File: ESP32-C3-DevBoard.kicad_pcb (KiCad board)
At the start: 2 copper layers, 25.4 x 26.7 mm, 19 parts, among them J1 USB_C_Receptacle_USB2.0, J2 Conn_01x10, J3 Conn_01x10, SW1 SW_Push, SW2 SW_Push, U1 ESP32-C3-WROOM-02, U2 AMS1117-3.3

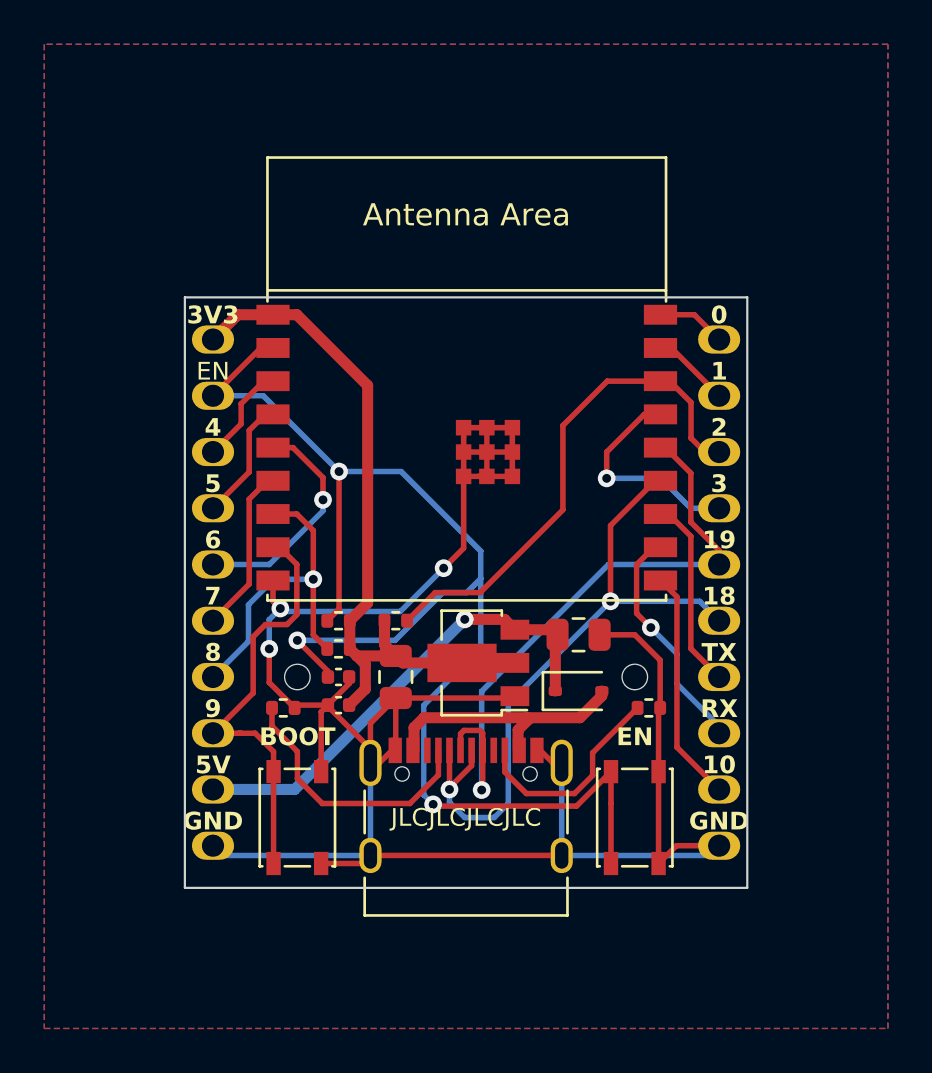
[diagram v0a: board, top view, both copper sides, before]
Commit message: fix silkscreen and tooling hole position
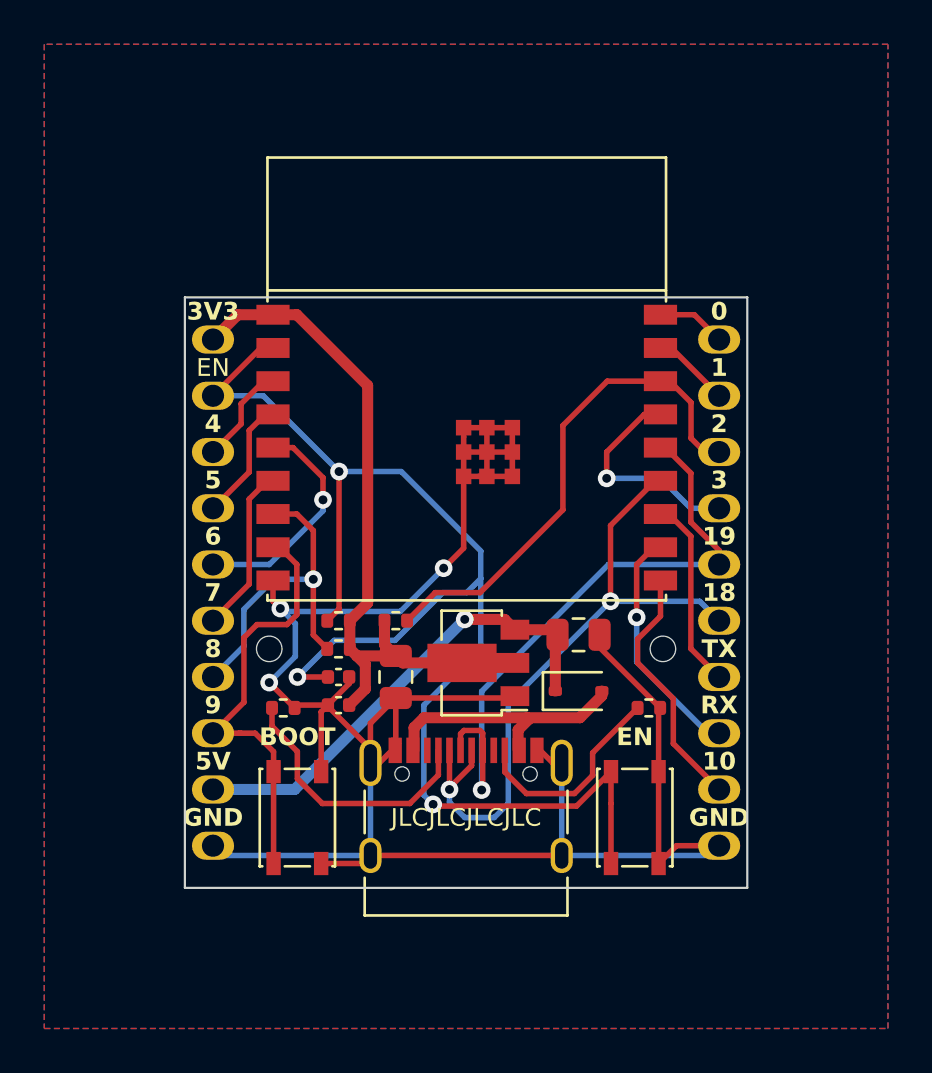
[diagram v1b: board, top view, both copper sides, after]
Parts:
- moved H1 1.80 mm to (137.2, 113.7)
- moved H2 1.80 mm to (154.9, 113.7)
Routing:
- net /IO10: track 10.5 -> 11.4 mm

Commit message: Add files via upload
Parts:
- H1, H2: value MountingHole -> ToolingHole
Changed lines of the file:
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@@
   (title_block
     (title "ESP32-C3 Development Board")
-    (rev "v1.0.0")
+    (rev "v1.0.1")
   )
   (layers
@@
     (pad "2" smd roundrect (at 0.51 0) (size 0.54 0.64) (layers "F.Cu" "F.Paste" "F.Mask") (roundrect_rratio 0.25)
       (net 15 "/IO2") (pintype "passive"))
-    (model "${KICAD6_3DMODEL_DIR}/Resistor_SMD.3dshapes/R_0402_1005Metric.wrl"
+    (model "${KICAD7_3DMODEL_DIR}/Resistor_SMD.3dshapes/R_0402_1005Metric.wrl"
       (offset (xyz 0 0 0))
       (scale (xyz 1 1 1))
@@
     (pad "2" smd roundrect (at 0.51 0 180) (size 0.54 0.64) (layers "F.Cu" "F.Paste" "F.Mask") (roundrect_rratio 0.25)
       (net 6 "/IO8") (pintype "passive"))
-    (model "${KICAD6_3DMODEL_DIR}/Resistor_SMD.3dshapes/R_0402_1005Metric.wrl"
+    (model "${KICAD7_3DMODEL_DIR}/Resistor_SMD.3dshapes/R_0402_1005Metric.wrl"
       (offset (xyz 0 0 0))
       (scale (xyz 1 1 1))
@@
     (pad "2" smd roundrect (at 0.95 0 270) (size 1 1.45) (layers "F.Cu" "F.Paste" "F.Mask") (roundrect_rratio 0.25)
       (net 8 "GND") (pintype "passive"))
-    (model "${KICAD6_3DMODEL_DIR}/Capacitor_SMD.3dshapes/C_0805_2012Metric.wrl"
+    (model "${KICAD7_3DMODEL_DIR}/Capacitor_SMD.3dshapes/C_0805_2012Metric.wrl"
       (offset (xyz 0 0 0))
       (scale (xyz 1 1 1))
@@
     (pad "2" smd roundrect (at 0.48 0) (size 0.56 0.62) (layers "F.Cu" "F.Paste" "F.Mask") (roundrect_rratio 0.25)
       (net 18 "+3V3") (pintype "passive"))
-    (model "${KICAD6_3DMODEL_DIR}/Capacitor_SMD.3dshapes/C_0402_1005Metric.wrl"
+    (model "${KICAD7_3DMODEL_DIR}/Capacitor_SMD.3dshapes/C_0402_1005Metric.wrl"
       (offset (xyz 0 0 0))
       (scale (xyz 1 1 1))
@@
     (pad "2" smd roundrect (at 0.51 0) (size 0.54 0.64) (layers "F.Cu" "F.Paste" "F.Mask") (roundrect_rratio 0.25)
       (net 8 "GND") (pintype "passive"))
-    (model "${KICAD6_3DMODEL_DIR}/Resistor_SMD.3dshapes/R_0402_1005Metric.wrl"
+    (model "${KICAD7_3DMODEL_DIR}/Resistor_SMD.3dshapes/R_0402_1005Metric.wrl"
       (offset (xyz 0 0 0))
       (scale (xyz 1 1 1))
@@
         (effects (font (size 1 1) (thickness 0.15)))
     )
-    (fp_text value "MountingHole" (at 0 3.2) (layer "F.Fab")
+    (fp_text value "ToolingHole" (at 0 3.2) (layer "F.Fab")
         (effects (font (size 1 1) (thickness 0.15)))
     )
@@
         (effects (font (size 1 1) (thickness 0.15)))
     )
-    (fp_text user "Antenna Area" (at 0 -10.4) (layer "F.SilkS") hide
+    (fp_text user "Antenna Area" (at 0 -10.4) (layer "F.SilkS")
         (effects (font (size 1 1) (thickness 0.15)))
     )
@@
     (pad "2" smd roundrect (at 0.95 0 180) (size 1 1.45) (layers "F.Cu" "F.Paste" "F.Mask") (roundrect_rratio 0.25)
       (net 19 "+5V") (pintype "passive"))
-    (model "${KICAD6_3DMODEL_DIR}/Capacitor_SMD.3dshapes/C_0805_2012Metric.wrl"
+    (model "${KICAD7_3DMODEL_DIR}/Capacitor_SMD.3dshapes/C_0805_2012Metric.wrl"
       (offset (xyz 0 0 0))
       (scale (xyz 1 1 1))
@@
     (pad "2" smd roundrect (at 0.48 0) (size 0.56 0.62) (layers "F.Cu" "F.Paste" "F.Mask") (roundrect_rratio 0.25)
       (net 8 "GND") (pintype "passive"))
-    (model "${KICAD6_3DMODEL_DIR}/Capacitor_SMD.3dshapes/C_0402_1005Metric.wrl"
+    (model "${KICAD7_3DMODEL_DIR}/Capacitor_SMD.3dshapes/C_0402_1005Metric.wrl"
       (offset (xyz 0 0 0))
       (scale (xyz 1 1 1))
@@
         (effects (font (size 1 1) (thickness 0.15)))
     )
-    (fp_text value "MountingHole" (at 0 3.2) (layer "F.Fab")
+    (fp_text value "ToolingHole" (at 0 3.2) (layer "F.Fab")
         (effects (font (size 1 1) (thickness 0.15)))
     )
@@
     (pad "2" smd roundrect (at 1.05 0) (size 0.6 0.45) (layers "F.Cu" "F.Paste" "F.Mask") (roundrect_rratio 0.25)
       (net 20 "VBUS") (pinfunction "A") (pintype "passive"))
-    (model "${KICAD6_3DMODEL_DIR}/Diode_SMD.3dshapes/D_SOD-323.wrl"
+    (model "${KICAD7_3DMODEL_DIR}/Diode_SMD.3dshapes/D_SOD-323.wrl"
       (offset (xyz 0 0 0))
       (scale (xyz 1 1 1))
@@
     (pad "2" smd roundrect (at 0.51 0 180) (size 0.54 0.64) (layers "F.Cu" "F.Paste" "F.Mask") (roundrect_rratio 0.25)
       (net 1 "/EN") (pintype "passive"))
-    (model "${KICAD6_3DMODEL_DIR}/Resistor_SMD.3dshapes/R_0402_1005Metric.wrl"
+    (model "${KICAD7_3DMODEL_DIR}/Resistor_SMD.3dshapes/R_0402_1005Metric.wrl"
       (offset (xyz 0 0 0))
       (scale (xyz 1 1 1))
@@
     (pad "2" smd roundrect (at 0.51 0 180) (size 0.54 0.64) (layers "F.Cu" "F.Paste" "F.Mask") (roundrect_rratio 0.25)
       (net 23 "Net-(J1-CC2)") (pintype "passive"))
-    (model "${KICAD6_3DMODEL_DIR}/Resistor_SMD.3dshapes/R_0402_1005Metric.wrl"
+    (model "${KICAD7_3DMODEL_DIR}/Resistor_SMD.3dshapes/R_0402_1005Metric.wrl"
       (offset (xyz 0 0 0))
       (scale (xyz 1 1 1))
@@
     (pad "3" smd rect (at -1.95 1.5 180) (size 1.3 0.9) (layers "F.Cu" "F.Paste" "F.Mask")
       (net 19 "+5V") (pinfunction "VI") (pintype "power_in"))
-    (model "${KICAD6_3DMODEL_DIR}/Package_TO_SOT_SMD.3dshapes/SOT-89-3.wrl"
+    (model "${KICAD7_3DMODEL_DIR}/Package_TO_SOT_SMD.3dshapes/SOT-89-3.wrl"
       (offset (xyz 0 0 0))
       (scale (xyz 1 1 1))
@@
     (pad "10" thru_hole oval (at 0 -22.86 180) (size 1.905 1.27) (drill 1) (layers "*.Cu" "*.Mask")
       (net 8 "GND") (pinfunction "Pin_10") (pintype "passive"))
-    (model "${KICAD6_3DMODEL_DIR}/Connector_PinHeader_2.54mm.3dshapes/PinHeader_1x10_P2.54mm_Vertical.wrl"
+    (model "${KICAD7_3DMODEL_DIR}/Connector_PinHeader_2.54mm.3dshapes/PinHeader_1x10_P2.54mm_Vertical.wrl"
       (offset (xyz 0 0 0))
       (scale (xyz 1 1 1))
@@
     (pad "10" thru_hole oval (at 0 -22.86 180) (size 1.905 1.27) (drill 1) (layers "*.Cu" "*.Mask")
       (net 8 "GND") (pinfunction "Pin_10") (pintype "passive"))
-    (model "${KICAD6_3DMODEL_DIR}/Connector_PinHeader_2.54mm.3dshapes/PinHeader_1x10_P2.54mm_Vertical.wrl"
-      (offset (xyz 0 0 0))
-      (scale (xyz 1 1 1))
+    (model "${KICAD7_3DMODEL_DIR}/Connector_PinHeader_2.54mm.3dshapes/PinHeader_1x10_P2.54mm_Vertical.wrl"
+      (offset (xyz 0 0 0))
+      (scale (xyz 1 1 1))

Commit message: Add Tooling Hole Library
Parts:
- H1, H2: footprint MountingHole:MountingHole_2.2mm_M2 -> Tooling_Hole:Tooling_Hole
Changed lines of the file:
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@@
     )
   )
-  (footprint "MountingHole:MountingHole_2.2mm_M2" (layer "F.Cu")
+  (footprint "Tooling_Hole:Tooling_Hole" (layer "F.Cu")
     (at 137.16 113.665)
-    (descr "Mounting Hole 2.2mm, no annular, M2")
-    (tags "mounting hole 2.2mm no annular m2")
     (property "Sheetfile" "ESP32-C3-DevBoard.kicad_sch")
     (property "Sheetname" "")
@@
     (property "ki_description" "Mounting Hole without connection")
     (property "ki_keywords" "mounting hole")
-    (attr exclude_from_pos_files exclude_from_bom allow_missing_courtyard)
-    (fp_text reference "H1" (at 0 -3.2) (layer "F.SilkS") hide
-        (effects (font (size 1 1) (thickness 0.15)))
-    )
-    (fp_text value "ToolingHole" (at 0 3.2) (layer "F.Fab")
-        (effects (font (size 1 1) (thickness 0.15)))
-    )
-    (fp_text user "${REFERENCE}" (at 0 0) (layer "F.Fab")
+    (attr exclude_from_bom)
+    (fp_text reference "H1" (at 0 -1.27 unlocked) (layer "F.SilkS") hide
+        (effects (font (size 1 1) (thickness 0.15)))
+    )
+    (fp_text value "ToolingHole" (at 0 1 unlocked) (layer "F.Fab")
+        (effects (font (size 1 1) (thickness 0.15)))
+    )
+    (fp_text user "${REFERENCE}" (at 0 2.5 unlocked) (layer "F.Fab")
         (effects (font (size 1 1) (thickness 0.15)))
     )
@@
     )
   )
-  (footprint "MountingHole:MountingHole_2.2mm_M2" (layer "F.Cu")
+  (footprint "Tooling_Hole:Tooling_Hole" (layer "F.Cu")
     (at 154.94 113.665)
-    (descr "Mounting Hole 2.2mm, no annular, M2")
-    (tags "mounting hole 2.2mm no annular m2")
     (property "Sheetfile" "ESP32-C3-DevBoard.kicad_sch")
     (property "Sheetname" "")
@@
     (property "ki_description" "Mounting Hole without connection")
     (property "ki_keywords" "mounting hole")
-    (attr exclude_from_pos_files exclude_from_bom allow_missing_courtyard)
-    (fp_text reference "H2" (at 0 -3.2) (layer "F.SilkS") hide
-        (effects (font (size 1 1) (thickness 0.15)))
-    )
-    (fp_text value "ToolingHole" (at 0 3.2) (layer "F.Fab")
-        (effects (font (size 1 1) (thickness 0.15)))
-    )
-    (fp_text user "${REFERENCE}" (at 0 0) (layer "F.Fab")
-        (effects (font (size 1 1) (thickness 0.15)))
-    )
+    (attr exclude_from_bom)
+    (fp_text reference "H2" (at 0 -1.27 unlocked) (layer "F.SilkS") hide
+        (effects (font (size 1 1) (thickness 0.15)))
+    )
+    (fp_text value "ToolingHole" (at 0 1 unlocked) (layer "F.Fab")
+        (effects (font (size 1 1) (thickness 0.15)))
+    )
+    (fp_text user "${REFERENCE}" (at 0 2.5 unlocked) (layer "F.Fab")
+        (effects (font (size 1 1) (thickness 0.15)))
+    )

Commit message: Add files via upload
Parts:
- C2: value 10uF -> 22uF
- R1, R2: value 5.1KΩ -> 5.1kΩ
- R3, R4, R5: value 10K -> 10kΩ
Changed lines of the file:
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@@
         (effects (font (size 1 1) (thickness 0.15)))
     )
-    (fp_text value "10K" (at 0 1.17) (layer "F.Fab")
+    (fp_text value "10kΩ" (at 0 1.17) (layer "F.Fab")
         (effects (font (size 1 1) (thickness 0.15)))
     )
@@
         (effects (font (size 1 1) (thickness 0.15)))
     )
-    (fp_text value "10K" (at 0 1.17) (layer "F.Fab")
+    (fp_text value "10kΩ" (at 0 1.17) (layer "F.Fab")
         (effects (font (size 1 1) (thickness 0.15)))
     )
@@
     (descr "Capacitor SMD 0805 (2012 Metric), square (rectangular) end terminal, IPC_7351 nominal, (Body size source: IPC-SM-782 page 76, https://www.pcb-3d.com/wordpress/wp-content/uploads/ipc-sm-782a_amendment_1_and_2.pdf, https://docs.google.com/spreadsheets/d/1BsfQQcO9C6DZCsRaXUlFlo91Tg2WpOkGARC1WS5S8t0/edit?usp=sharing), generated with kicad-footprint-generator")
     (tags "capacitor")
-    (property "LCSC" "C15850")
+    (property "LCSC" "C45783")
     (property "Sheetfile" "ESP32-C3-DevBoard.kicad_sch")
     (property "Sheetname" "")
@@
         (effects (font (size 1 1) (thickness 0.15)))
     )
-    (fp_text value "10uF" (at 0 1.68 90) (layer "F.Fab")
+    (fp_text value "22uF" (at 0 1.68 90) (layer "F.Fab")
         (effects (font (size 1 1) (thickness 0.15)))
     )
@@
         (effects (font (size 1 1) (thickness 0.15)))
     )
-    (fp_text value "5.1KΩ" (at 0 1.17) (layer "F.Fab")
+    (fp_text value "5.1kΩ" (at 0 1.17) (layer "F.Fab")
         (effects (font (size 1 1) (thickness 0.15)))
     )
@@
         (effects (font (size 1 1) (thickness 0.15)))
     )
-    (fp_text value "10K" (at 0 1.17) (layer "F.Fab")
+    (fp_text value "10kΩ" (at 0 1.17) (layer "F.Fab")
         (effects (font (size 1 1) (thickness 0.15)))
     )
@@
         (effects (font (size 1 1) (thickness 0.15)))
     )
-    (fp_text value "5.1KΩ" (at 0 1.17) (layer "F.Fab")
-        (effects (font (size 1 1) (thickness 0.15)))
-    )
+    (fp_text value "5.1kΩ" (at 0 1.17) (layer "F.Fab")
+        (effects (font (size 1 1) (thickness 0.15)))
+    )

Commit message: Add files via upload
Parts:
- added JP1: Jumper_2_Open, Jumper:SolderJumper-2_P1.3mm_Open_RoundedPad1.0x1.5mm, B.Cu at (151.1, 115.6)
- added JP2: Jumper_2_Open, Jumper:SolderJumper-2_P1.3mm_Open_RoundedPad1.0x1.5mm, B.Cu at (141.7, 113.7)
- C2: footprint Capacitor_SMD:C_0805_2012Metric -> Capacitor_SMD:C_0603_1608Metric
- moved C2 0.13 mm to (142.9, 115.1)
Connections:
- C2 pad 1: +3V3 -> Net-(JP2-A)
- U2 pad 2: +3V3 -> Net-(JP2-A)
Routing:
- net +3V3: track 33.1 -> 25.7 mm, vias 0 -> 1
- net Net-(JP2-A): track 0.00 -> 5.30 mm, vias 0 -> 1
- net +5V: track 21.6 -> 22.8 mm, vias 1 -> 2
- net /EN: track 62.6 -> 61.7 mm
- net VBUS: track 12.3 -> 12.7 mm, vias 0 -> 1
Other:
- board text added: "DIODE"
- board text added: "POWER"

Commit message: Add files via upload
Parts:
- removed U2: AMS1117-3.3, Package_TO_SOT_SMD:SOT-89-3
- added U3: RT9080-33GJ5, Package_TO_SOT_SMD:SOT-23-5, F.Cu at (146.7, 113.7)
- JP2: value Jumper_2_Open -> Jumper_2_Bridged; footprint Jumper:SolderJumper-2_P1.3mm_Open_RoundedPad1.0x1.5mm -> Jumper:SolderJumper-2_P1.3mm_Bridged_RoundedPad1.0x1.5mm
- moved JP1 2.05 mm to (150.4, 113.7)
- moved J1 1.27 mm to (146.1, 120.7)
- moved C4 0.89 mm to (140.3, 115.3)
- moved C2 0.76 mm to (142.9, 114.3)
- moved R1 0.76 mm to (137.8, 115.6)
- moved R2 0.76 mm to (154.3, 115.6)
- moved C3 0.64 mm to (140.3, 114.3)
- moved D1 0.63 mm to (151.1, 114.9)
- moved SW1 0.63 mm to (138.4, 120.7)
- moved SW2 0.63 mm to (153.7, 120.7)
- moved R4 0.38 mm to (140.3, 113.3)
- moved C1 0.13 mm to (151.1, 112.9)
- moved R3 0.13 mm to (142.9, 112.3)
- moved R5 0.13 mm to (140.3, 112.3)
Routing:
- net /IO19: track 28.5 -> 36.2 mm, vias 1 -> 2
- net /IO18: track 31.1 -> 38.3 mm
- net Net-(JP2-A): track 5.30 -> 3.12 mm
- net Net-(J1-CC2): track 9.57 -> 11.0 mm
- net /IO10: track 11.4 -> 12.2 mm
- net /IO9: track 19.5 -> 18.9 mm
- net Net-(J1-CC1): track 12.1 -> 12.7 mm
- net GND: track 105.7 -> 105.9 mm, vias 3 -> 4
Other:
- board size 25.4 x 26.7 mm -> 25.4 x 26 mm
